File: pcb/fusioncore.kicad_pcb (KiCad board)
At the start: 2 copper layers, 95 x 99 mm, 114 parts, among them J1 40HAT, J10 Pump_Misc_1, J11 Pump_Misc_2, J12 I2C_DBG, J13 Conn_02x03_Top_Bottom, J14 LED, J15 Trigger, J16 WEIGHT, J17 Valve_M1, J18 Valve_M2, J19 Valve_M3, J2 Conn_02x12_Top_Bottom, J20 Valve_M4, J21 Valve_Air_Lime, J22 Valve_Air_Rum, J23 Valve_Air_Out, J3 Flow_Warm, J4 Temperature, J5 Flow_Cold, J6 CONN_01X02, J7 Pump_Cold, J8 Pump_Warm, J9 Pump_Air, Q1 DMG2305UX, Q10 AO3400A, Q11 AO3400A, Q2 DMMT5401, Q3 AO3400A, Q4 AO3400A, Q5 AO3400A, Q6 AO3400A, Q7 AO3400A, Q8 MMBT4403, Q9 AO3400A, SW1 POWER_ON, U1 CAT24C32, U2 INA226, U3 INA226, U4 INA226, U5 TXB0108DQSR, U6 HX711

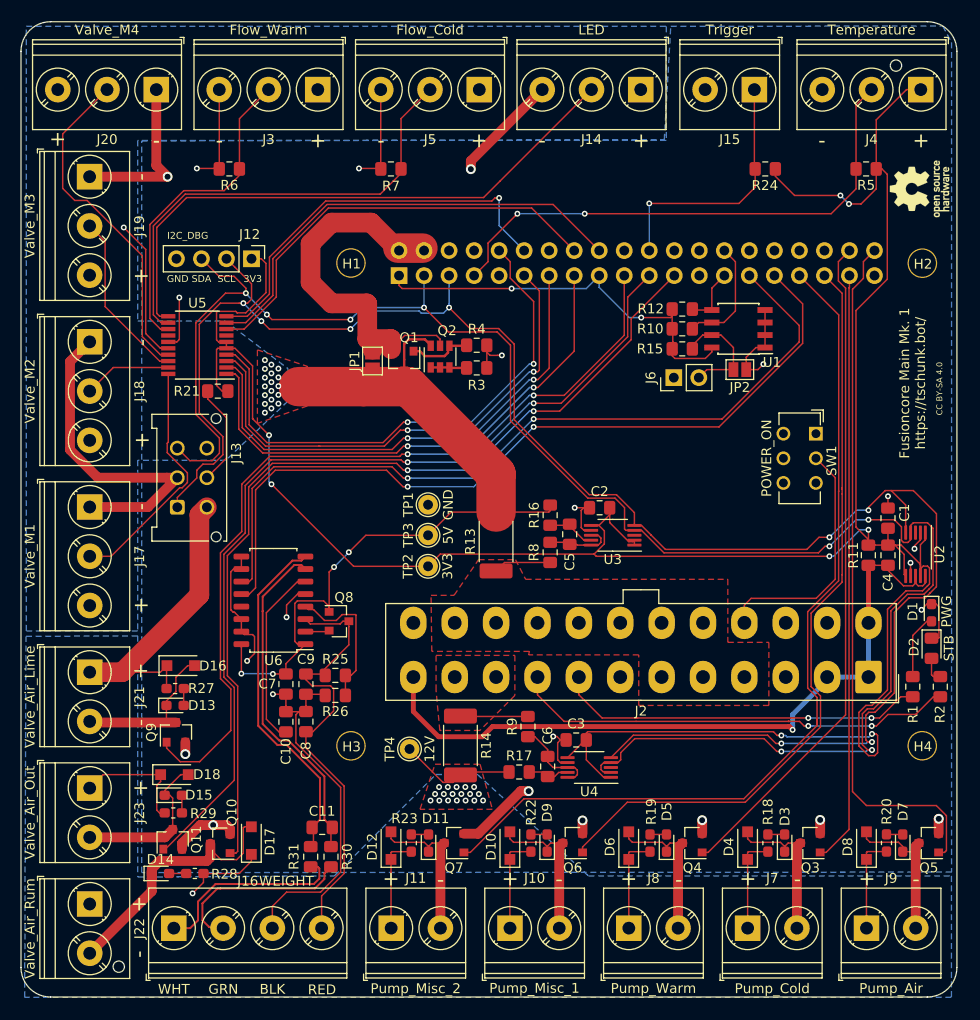
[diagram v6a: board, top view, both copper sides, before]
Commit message: Added a P82B96TD for external HighVoltage I2C
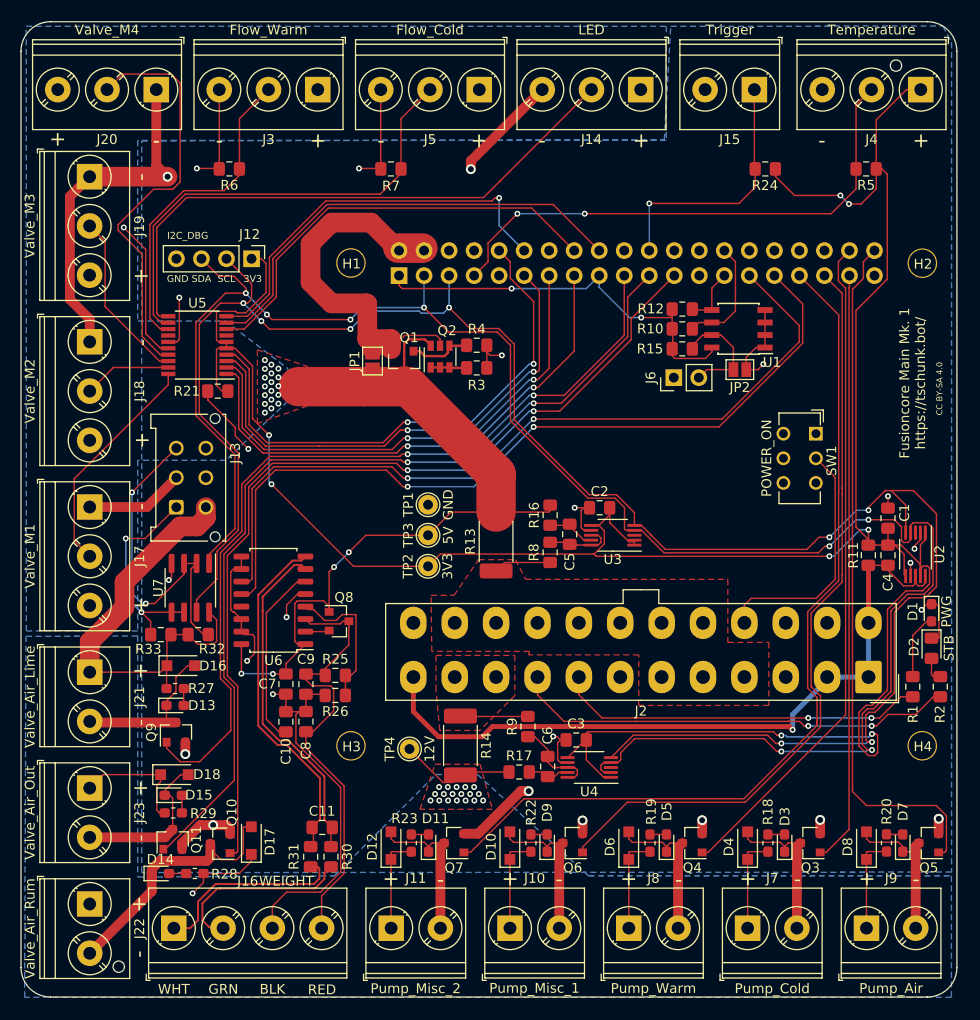
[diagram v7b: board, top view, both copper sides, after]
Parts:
- removed REF**: OSHW-Logo_5.7x6mm_SilkScreen, Symbol:OSHW-Logo_5.7x6mm_SilkScreen
- added R32: 200, Resistor_SMD:R_0805_2012Metric_Pad1.15x1.40mm_HandSolder, F.Cu at (66.5, 102.0)
- added R33: 200, Resistor_SMD:R_0805_2012Metric_Pad1.15x1.40mm_HandSolder, F.Cu at (62.7, 102.0)
- added U7: P82B96, Package_SO:SOIC-8_3.9x4.9mm_P1.27mm, F.Cu at (65.7, 97.3)
- moved J13 0.10 mm to (64.3, 89.1)
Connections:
- J13 pad 1: /I2C_SCL -> Net-(J13-Pad1)
- J13 pad 3: /I2C_SDA -> Net-(J13-Pad3)
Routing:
- net Net-(J13-Pad3): track 0.00 -> 34.4 mm, vias 0 -> 2
- net Net-(J13-Pad1): track 0.00 -> 21.6 mm, vias 0 -> 2
- net /12V: track 117.1 -> 128.6 mm
- net /I2C_SCL: track 189.2 -> 199.7 mm
- net /Valve_M4_5V: track 34.4 -> 42.3 mm
- net /I2C_SDA: track 187.2 -> 195.0 mm
- net GND: track 210.1 -> 203.6 mm, vias 23 -> 25
- net /Valve_M1_5V: track 24.9 -> 23.1 mm
